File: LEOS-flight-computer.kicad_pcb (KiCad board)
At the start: 2 copper layers, 100 x 100 mm, 29 parts, among them J1 MicroFit_1x4, J2 MicroFit_1x4, J3 GPIO, J4 I2C Breakout, J5 SPI Breakout, U1 MCP2562FD, U2 MCP2518FD, U3 SAM-M8Q, Y1 40 MHz

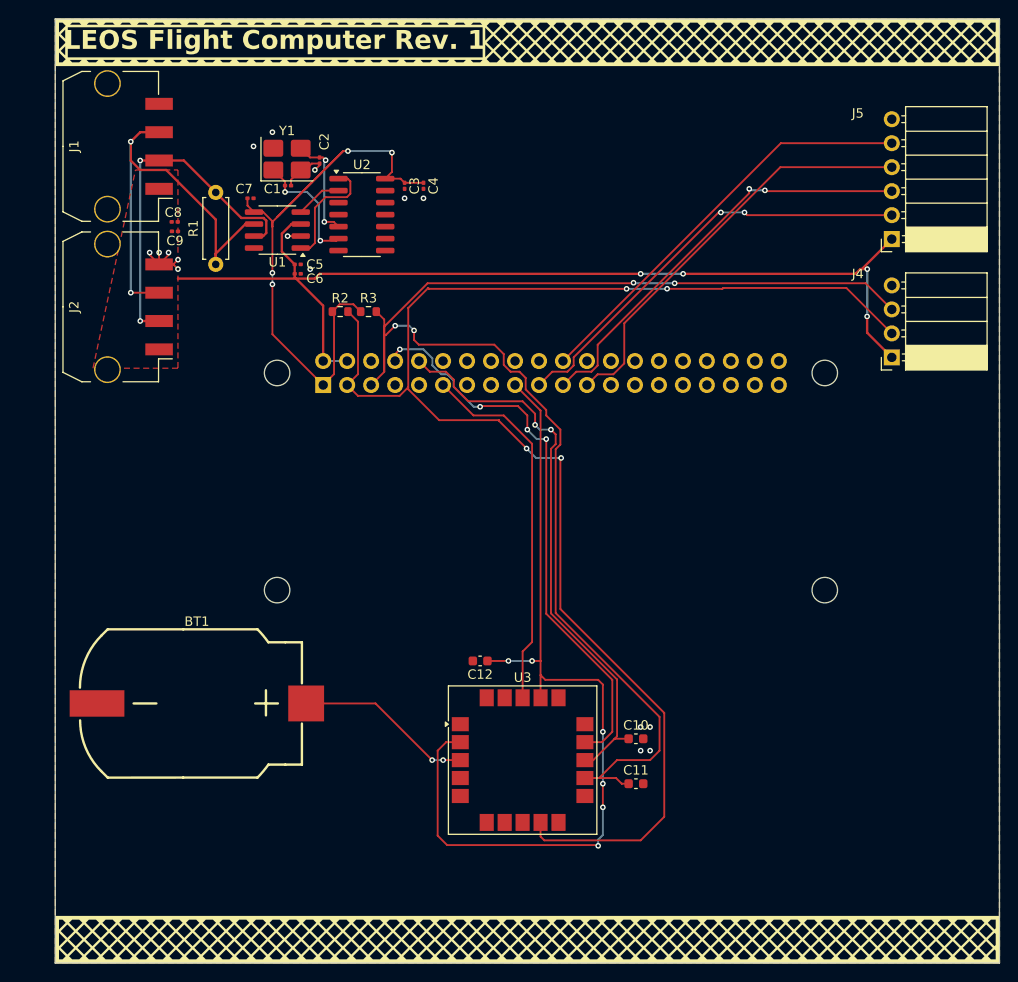
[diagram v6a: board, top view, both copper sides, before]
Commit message: Added labels and CANBus SPI connections
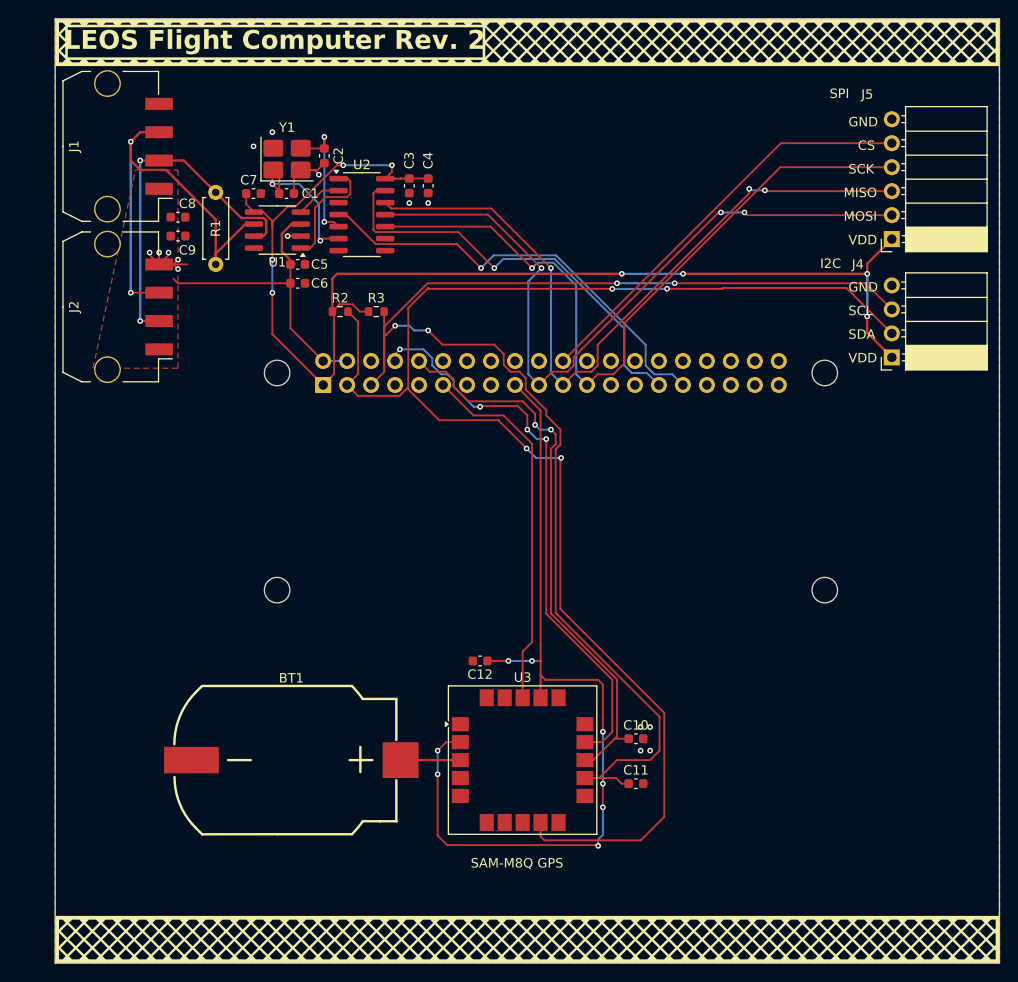
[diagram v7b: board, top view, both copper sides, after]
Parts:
- BT1: value CR2032_Battery_Cell -> Battery_Cell
- C1, C2, C3, C4, C5, C6, C7, C8, C9: footprint Capacitor_SMD:C_0201_0603Metric -> Capacitor_SMD:C_0603_1608Metric
- moved BT1 11.7 mm to (125.5, 128.5)
- moved C6 1.00 mm to (125.7, 78.0)
- moved C1 0.86 mm to (124.5, 68.5)
- moved R3 0.82 mm to (134.0, 81.0)
- moved C2 0.71 mm to (128.5, 64.5)
- moved C8 0.61 mm to (113.0, 71.0)
- moved C7 0.59 mm to (121.0, 68.5)
- moved C9 0.59 mm to (113.0, 73.0)
- moved C3 0.50 mm to (137.5, 67.7)
- moved C4 0.50 mm to (139.5, 67.7)
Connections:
- J4 pad 1: +5V -> VDD
- J5 pad 1: +5V -> VDD
- U2 pad 10: /CAN_SCK -> GPIO11/SPI0.SCLK
- U2 pad 11: /CAN_MOSI -> GPIO10/SPI0.MOSI
- U2 pad 12: /CAN_MISO -> GPIO9/SPI0.MISO
- U2 pad 13: /CAN_CS -> GPIO5
- U2 pad 4: /CAN_INT -> GPIO6
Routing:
- net +5V: track 108.8 -> 33.1 mm, vias 4 -> 0
- net VDD: track 162.5 -> 227.4 mm, vias 10 -> 16
- net GPIO6: track 0.00 -> 46.3 mm, vias 0 -> 1
- net GPIO5: track 0.00 -> 45.4 mm, vias 0 -> 1
- net GPIO11/SPI0.SCLK: track 44.3 -> 78.6 mm, vias 0 -> 1
- net GPIO9/SPI0.MISO: track 45.1 -> 78.4 mm, vias 2 -> 3
- net GPIO10/SPI0.MOSI: track 45.6 -> 77.9 mm, vias 2 -> 3
- net Net-(BT1-+): track 18.8 -> 6.33 mm, vias 2 -> 0
- net GND: track 14.1 -> 19.6 mm, vias 16 -> 15
- net /OSC1: track 12.9 -> 17.7 mm
- net /OSC2: track 11.5 -> 14.4 mm
- net GPIO3/SCL1: track 147.5 -> 146.5 mm
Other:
- board text added: "CS"
- board text added: "GND"
- board text added: "I2C"
- board text added: "LEOS Flight Computer Rev. 2"
- board text added: "MISO"
- board text added: "MOSI"
- board text added: "SAM-M8Q GPS"
- board text added: "SCK"
- board text added: "SCL"
- board text added: "SDA"
- board text added: "SPI"
- board text added: "VDD"
- board text removed: "LEOS Flight Computer Rev. 1"

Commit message: Final updates before production - Includes GARY.
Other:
- board text added: "GARY."
